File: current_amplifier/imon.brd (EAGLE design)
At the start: 160 x 100 mm, 32 parts, among them U1 AD8210, U2 AD1583_AD1583BRTZ-REEL7CT-ND, U3 FR014H5JZ, U4 OP-AMP_BALANCED, U6 LTC2312-12

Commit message: The imon current monitor board schematic is filled out
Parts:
- removed C1, C16, R2: (no value), rcl_custom:.0805-B
- removed U1: AD8210, marionette:SOIC-8_NARROW_BODY
- removed U3: FR014H5JZ, marionette:MLP-3X3
- added C105, C19: 1u, rcl_custom:.0402-B
- added C18, R12, R13, R19: np, rcl_custom:.0402-B
- added C20: 6.2n, rcl_custom:.0402-B
- added C50: 220p, rcl_custom:.0402-B
- added C80: 100n, rcl_custom:.0402-B
- added D1, D2: ESD8006-ESD8006, marionette:UDFN-8-3.3X1.0_6MIL
- added J1, R11, R16, R17: (no value), marionette:JUMPER-SHORTED-CUTTABLE-E0402-0.3MM
- added R10: 56, rcl_custom:.0402-B
- added R18: 1k, rcl_custom:.0402-B
- added R30: 51, rcl_custom:.0402-B
- added R40: 560, rcl_custom:.0402-B
- added R67, R9: np, rcl_custom:1206-0402
- added TP1, TP10, TP11, TP9: PAD+VIA_0.25MM, marionette:PAD+VIA_0.25MM
- added TP2: PAD+VIA_0.6MM, marionette:PAD+VIA_0.6MM
- added TP3, TP4, TP5, TP6, TP7, TP8: (no value), marionette:PAD-ROUND-1.0-NOCREAM+SILK
- added U$1: MCP1501", marionette:SOT23-6
- C10, C3: value (none) -> 100n; device rcl_custom:.0805-B -> rcl_custom:.0402-B
- C11, C12, C13, C14, C15, C4: value (none) -> 1u; device rcl_custom:.0805-B -> rcl_custom:.0402-B
- C2: value (none) -> 2.7n; device rcl_custom:.0805-B -> rcl_custom:.0402-B
- C5: value (none) -> 220p; device rcl_custom:.0805-B -> rcl_custom:.0402-B
- C6, C7: value (none) -> 1u; device rcl_custom:.0805-A-NOSILK -> rcl_custom:.0402-B
- C9: value (none) -> np
- R1: value (none) -> 97.6; device rcl_custom:.0805-B -> rcl_custom:.0402-B
- R3: value (none) -> 88.7; device rcl_custom:.0805-B -> rcl_custom:.0402-B
- R4: value (none) -> 976; device rcl_custom:.0805-B -> rcl_custom:.0402-B
- R5, R6: device rcl_custom:.0805-B -> rcl_custom:.0402-B
- R7, R8: device rcl_custom:.0805-B -> rcl_custom:1206-0402
- U2: value AD1583_AD1583BRTZ-REEL7CT-ND -> OPAMP_DUALFAN4852; device marionette:SOT23-3 -> marionette:MSOP-8
- U4: value OP-AMP_BALANCED -> AD8418; device marionette:SOIC-8 -> marionette:SOIC-8_BETTER_TOE
- moved R4 198.5 mm to (-69.8, -218.4)
- moved R5 167.5 mm to (-63.5, -191.8)
- moved R6 167.5 mm to (-63.5, -195.6)
- moved C2 164.9 mm to (-63.5, -170.2)
- moved R1 153.6 mm to (-63.5, -162.6)
- moved R3 142.3 mm to (-63.5, -158.8)
- moved C7 141.2 mm to (-63.5, -188.0)
- moved U2 137.0 mm to (-68.6, -212.1)
- moved C6 134.9 mm to (-63.5, -177.8)
- moved C5 127.2 mm to (-63.5, -166.4)
- moved C15 125.9 mm to (-63.5, -203.2)
- moved C14 125.9 mm to (-63.5, -199.4)
- moved U4 117.7 mm to (-57.1, -113.0)
- moved C4 112.1 mm to (-63.5, -147.3)
- moved C3 112.1 mm to (-63.5, -143.5)
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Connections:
- removed net N$15: R7.1, U1.8
- removed net N$7: R6.1, U4.5
- new net C80: C6.2, C80.2, U4.2
- new net N$11: R8.1, U4.1
- new net N$16: R5.2, R6.1, U$1.4
- new net N$17: C50.1, R30.1, U2.6
- new net N$18: C50.2, R16.2, R40.1, TP5.PAD, U2.7
- new net N$19: C18.2, R16.1, R17.2, U6.4
- new net N$20: D2.4, JP2.1, R11.2
- new net N$21: J1.1, R19.1, TP9.TP, U4.3
- new net N$22: R12.1, TP1.TP
- new net VREF_FILTERED: C105.2, C7.2, J1.2, R12.2, R13.1, R18.2, TP10.TP, TP11.TP, U4.7
- new net VREF_OUT: R18.1, U$1.1
- net GND: now also C105.1, C14.1, C15.1, C18.1, C19.2, C2.1, C20.1, C7.1, D1.10, D1.3, D1.6, D1.9, D2.10, D2.3, D2.6, D2.9, R13.2, R19.2, R5.1, U$1.2, U$1.3, U$1.5, U2.3, U2.4, U2.5; no longer C1.2, C14.2, C15.2, C16.1, C5.2, R3.1, R5.2, R6.2, U1.2, U1.3, U2.2, U4.4
- net N$1: now also R1.2, R11.1, TP3.PAD, U4.5; no longer JP2.1, R1.1, U1.5
- net N$10: now also R67.1, R8.2, R9.1; no longer C6.1, C7.1, R7.2
- net N$12: now also D1.4, TP8.PAD
- net N$13: now also D1.2, TP7.PAD
- net N$14: now also D1.1, TP6.PAD
- net N$2: now also C2.2, R1.1, R3.2, R4.2; no longer C1.1, C2.1, R1.2, R2.1
- net N$3: now also C5.1, R3.1, U2.2; no longer R2.2, U4.3
- net N$4: now also C5.2, R10.2, R4.1, TP4.PAD, U2.1; no longer R3.2, R4.2, U4.2
- net N$5: now also D2.1, R17.1; no longer C2.2, R4.1, U4.6, U6.4
- net N$6: now also C20.2, R10.1, R30.2, R40.2; no longer R5.1, U4.1
- net N$8: now also R7.1, U4.8; no longer R8.1, U1.1
- net N$9: now also R67.2, R7.2, R9.2; no longer C6.2, C7.2, R8.2
- net V3.3D: now also C19.1, D1.7
- net V5D: now also C14.2, C15.2, C6.1, C80.1, D1.5, R6.2, U$1.6, U2.8, U4.6; no longer C14.1, C15.1, C16.2, C5.1, U1.6, U2.3, U4.7
- net VREF_3.0V: now also TP2.TP; no longer U1.7, U2.1

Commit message: laying out imon.brd
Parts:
- removed D2: ESD8006-ESD8006, marionette:UDFN-8-3.3X1.0_6MIL
- removed JP3: (no value), pinhead:1X07
- removed U$1: MCP1501", marionette:SOT23-6
- added FIDUCIAL1, FIDUCIAL2, FIDUCIAL3, FIDUCIAL4, FIDUCIAL5, FIDUCIAL6: FIDUCIAL-1.0X2.5, marionette:FIDUCIAL-1.0X2.5
- added R14: np, rcl_custom:.0402-B
- added R2: (no value), marionette:JUMPER-SHORTED-CUTTABLE-E0402-0.3MM
- added TP12, TP14: PAD+VIA_0.25MM, marionette:PAD+VIA_0.25MM
- added TP13: PAD+VIA_GND_0.25MM, marionette:PAD+GND_VIA_0.25MM
- added U5: MCP1501", marionette:SOT23-6
- C13: value 1u -> 10u; device rcl_custom:.0402-B -> rcl_custom:.0805-B
- C8, R5: value (none) -> np
- JP2: device pinhead:1X04 -> pinhead:2X12/90
- R6: value (none) -> 10k
- TP11: value PAD+VIA_0.25MM -> PAD+VIA_0.6MM; device marionette:PAD+VIA_0.25MM -> marionette:PAD+VIA_0.6MM
- TP3: value (none) -> PAD+VIA_GND_0.25MM; device marionette:PAD-ROUND-1.0-NOCREAM+SILK -> marionette:PAD+GND_VIA_0.25MM
- moved TP11 393.4 mm to (24.4, 30.8)
- moved C105 380.2 mm to (27.0, 26.0), flipped to the bottom, turned to 90 degrees
- moved TP1 378.3 mm to (30.6, 30.1)
- moved R19 365.8 mm to (25.2, 24.3), flipped to the bottom
- moved J1 363.9 mm to (25.8, 26.0), flipped to the bottom, turned to 90 degrees
- moved TP10 362.0 mm to (29.4, 30.1)
- moved C19 351.5 mm to (53.2, 24.5), flipped to the bottom
- moved TP9 345.4 mm to (25.6, 21.5)
- moved R18 340.5 mm to (29.4, 26.0), flipped to the bottom, turned to 90 degrees
- moved TP4 330.6 mm to (43.1, 30.5)
- moved TP3 324.4 mm to (31.9, 31.6)
- moved TP6 322.7 mm to (93.0, -9.00)
- moved TP7 322.5 mm to (93.0, -13.0)
- moved TP8 322.3 mm to (93.0, -17.0)
- moved TP5 321.0 mm to (91.0, -6.00)
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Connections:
- net N$10 renamed VSHUNT_M
- net N$11 renamed VSHUNT_FILTERED_M
- net N$17 renamed FILTER2-
- net N$18 renamed FILTER_2_OUT
- net N$2 renamed FILTER_1_V1
- net N$21 renamed AD8418_REF2
- net N$22 renamed VREF_OPTIONAL
- net N$3 renamed FILTER1-
- net N$4 renamed FILTER_1_OUT
- net N$6 renamed FILTER_2_V1
- net N$8 renamed VSHUNT_FILTERED_P
- net N$9 renamed VSHUNT_P
- net VREF_3.0V renamed ADC_VREF
- removed net C80: C6.2, C80.2, U4.2
- removed net N$1: R1.2, R11.1, TP3.PAD, U4.5
- removed net N$12: D1.4, JP3.5, TP8.PAD, U6.6
- removed net N$13: D1.2, JP3.6, TP7.PAD, U6.7
- removed net N$14: D1.1, JP3.7, TP6.PAD, U6.8
- removed net N$16: R5.2, R6.1, U$1.4
- removed net N$19: C18.2, R16.1, R17.2, U6.4
- removed net N$20: D2.4, JP2.1, R11.2
- removed net N$5: D2.1, JP2.3, R17.1
- new net ADC_AIN: R2.1, U6.4
- new net ADC_CONV: D1.1, JP2.21, JP2.22, TP6.PAD, U6.8
- new net ADC_SCK: D1.2, JP2.19, JP2.20, TP7.PAD, U6.7
- new net ADC_SDO: D1.4, JP2.17, JP2.18, TP8.PAD, U6.6
- new net MCP1501_SHDN_N: R5.2, R6.1, U5.4
- new net VSHUNT_20X: R1.2, R11.1, TP12.TP, U4.5
- new net VSHUNT_20X_OUT: D1.8, JP2.3, JP2.4, R11.2
- new net VSHUNT_FILTERED: D1.5, JP2.5, JP2.6, R17.1
- new net VSHUNT_FILTERED_ADC: C18.2, R14.1, R16.1, R17.2, R2.2, TP14.TP
- net GND: now also C6.2, C80.2, JP2.1, JP2.11, JP2.12, JP2.15, JP2.16, JP2.23, JP2.24, JP2.7, JP2.8, R14.2, TP13.TP, TP3.TP, U4.2, U5.2, U5.3, U5.5; no longer D2.10, D2.3, D2.6, D2.9, JP2.4, JP3.2, JP3.4, U$1.2, U$1.3, U$1.5
- net V3.3D: now also JP2.13, JP2.14; no longer JP3.3
- net V5D: now also JP2.10, JP2.9, U5.6; no longer D1.5, JP3.1, U$1.6
- net VREF_OUT: now also U5.1; no longer U$1.1

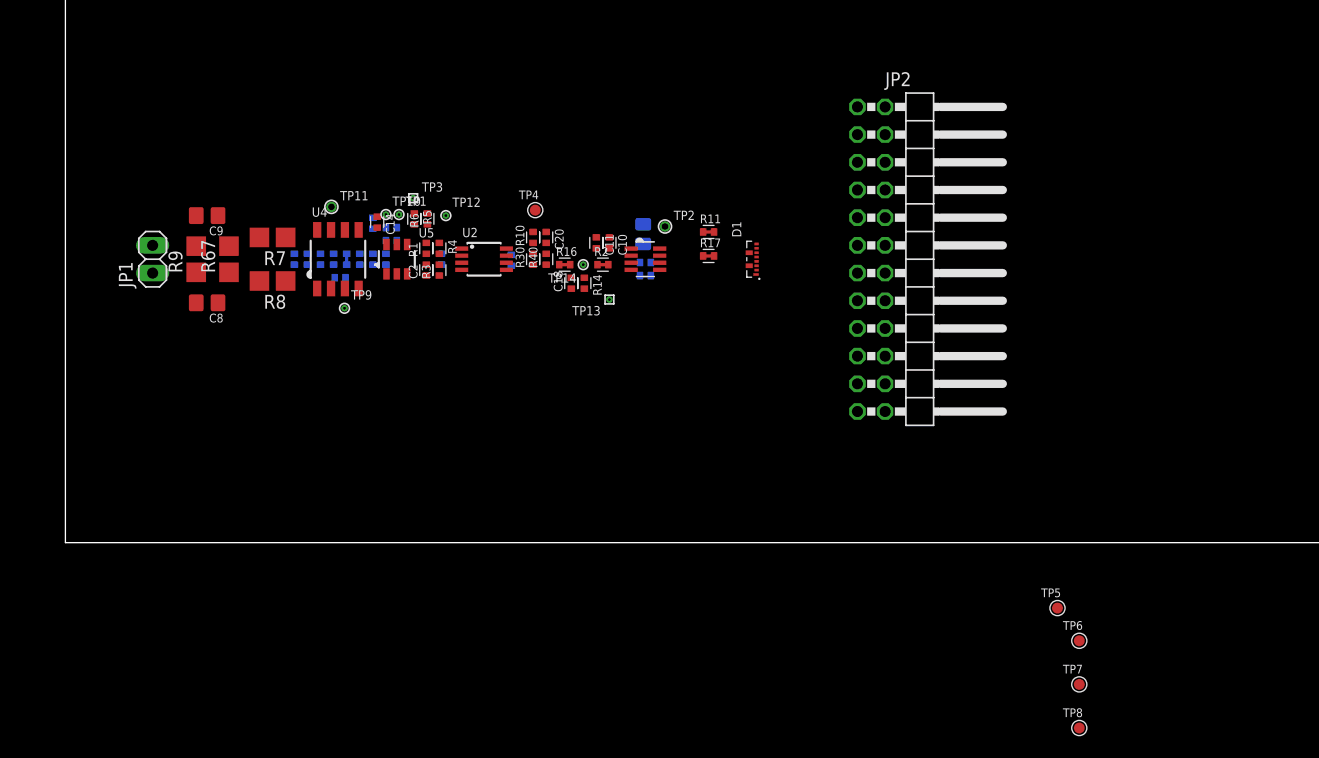
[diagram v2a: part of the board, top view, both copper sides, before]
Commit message: current monitor layout in progress
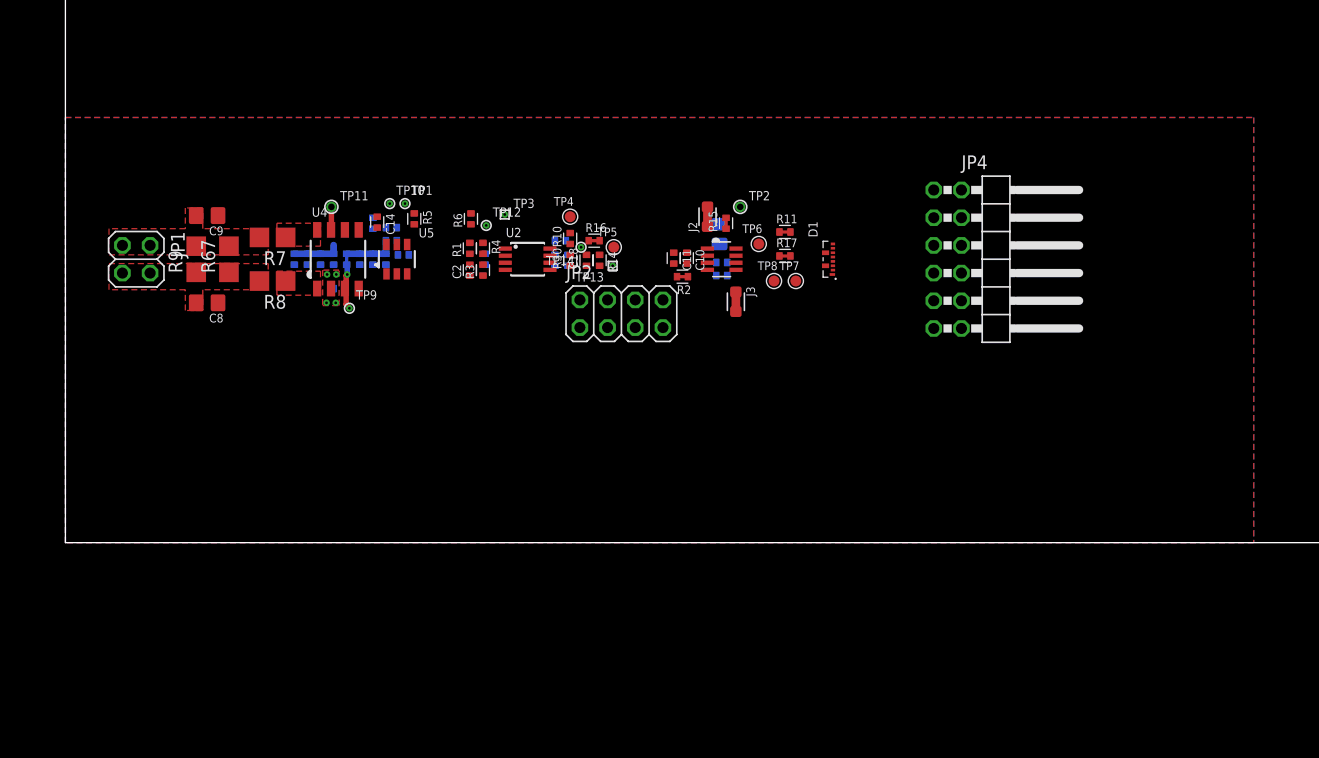
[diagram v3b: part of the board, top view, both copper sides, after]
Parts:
- added C1: 10n, rcl_custom:.0402-B
- added J2, J3: (no value), marionette:JUMPER-SHORTED-CUTTABLE-E0603-0.8MM
- added JP4: (no value), pinhead:2X06/90
- added R15: (no value), marionette:JUMPER-SHORTED-CUTTABLE-E0402-0.3MM
- JP1: device pinhead:1X02 -> pinhead:2X02
- JP2: device pinhead:2X12/90 -> pinhead:2X04
- moved TP5 52.5 mm to (50.3, 27.1)
- moved TP8 49.6 mm to (65.0, 24.0)
- moved TP6 46.8 mm to (63.6, 27.4)
- moved TP7 45.2 mm to (67.0, 24.0)
- moved JP2 28.4 mm to (51.0, 21.0), turned to 0 degrees
- moved TP3 8.53 mm to (40.3, 30.1)
- moved R2 7.38 mm to (56.6, 24.4), turned to 180 degrees
- moved C10 7.24 mm to (57.0, 26.1)
- moved C11 7.24 mm to (55.8, 26.1)
- moved TP2 7.13 mm to (61.9, 30.8)
- moved C12 7.00 mm to (60.2, 25.7)
- moved C13 7.00 mm to (60.0, 28.3)
- moved C19 7.00 mm to (60.2, 24.5)
- moved D1 7.00 mm to (70.0, 26.0)
- moved R11 7.00 mm to (66.0, 28.5)
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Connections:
- new net ADC_VREF_CUTTABLE: R15.1, U6.2
- new net V3.3D_CUTTABLE: J3.1, U6.5
- new net V5D_CUTTABLE: J2.1, U6.1
- net ADC_CONV: now also JP4.10, JP4.9; no longer JP2.21, JP2.22
- net ADC_SCK: now also JP4.7, JP4.8; no longer JP2.19, JP2.20
- net ADC_SDO: now also JP4.5, JP4.6; no longer JP2.17, JP2.18
- net ADC_VREF: now also R15.2; no longer U6.2
- net GND: now also C1.1, JP4.11, JP4.12; no longer JP2.1, JP2.11, JP2.12, JP2.15, JP2.16, JP2.2, JP2.23, JP2.24
- net V3.3D: now also J3.2, JP4.3, JP4.4; no longer JP2.13, JP2.14, U6.5
- net V5D: now also D1.8, J2.2, JP4.1, JP4.2; no longer JP2.10, JP2.9, U6.1
- net VREF_FILTERED: now also C1.2, JP2.5, JP2.6
- net VSHUNT_20X_OUT: now also JP2.1, JP2.2; no longer D1.8, JP2.3, JP2.4
- net VSHUNT_FILTERED: now also JP2.3, JP2.4; no longer D1.5, JP2.5, JP2.6
- net VSHUNT_M: now also JP1.3, JP1.4; no longer JP1.1
- net VSHUNT_P: now also JP1.1
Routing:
- net VREF_FILTERED: track 0.00 -> 6.94 mm
- net V5D: track 0.00 -> 4.42 mm
- net AD8418_REF2: track 0.00 -> 4.32 mm, vias 0 -> 1
- net GND: track 0.00 -> 0.20 mm, vias 0 -> 4
- added copper zone on layer 1, net GND
- added copper zone on layer 16, net GND
- added copper zone on layer 2, net GND
- added copper zone on layer 3, net N$1
- added copper zone on layer 1, net VSHUNT_FILTERED_M
- added copper zone on layer 1, net VSHUNT_FILTERED_P
- added copper zone on layer 1, net VSHUNT_M
- added copper zone on layer 1, net VSHUNT_P
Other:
- board text added: "Ground Clip Soldermask Areas"
- board text added: "Need some 1.1mm diameter vias for scope probes"

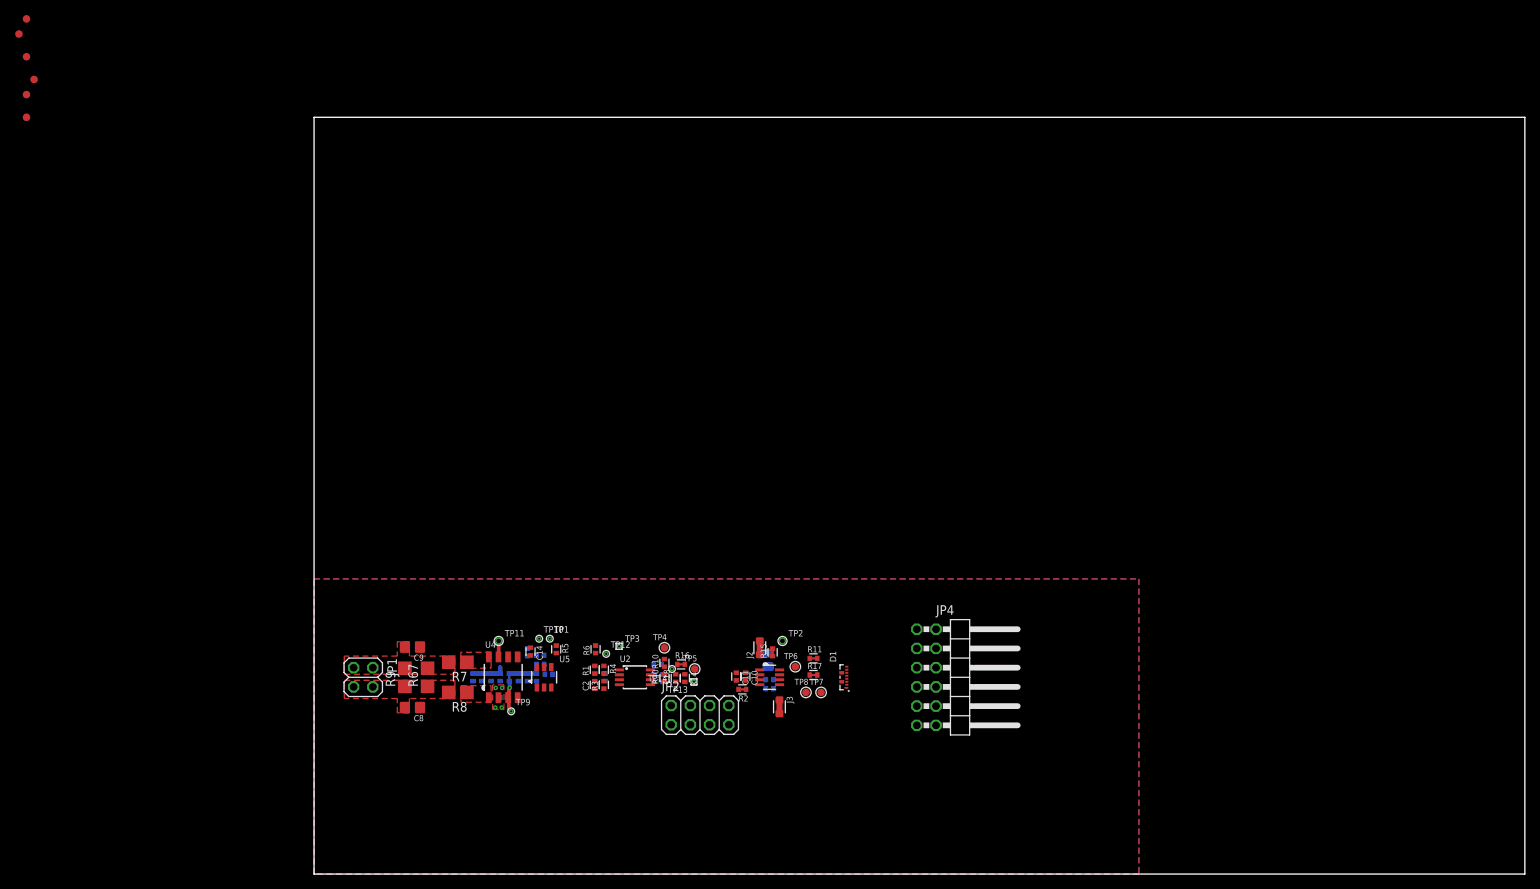
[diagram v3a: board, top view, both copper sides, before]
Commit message: The current monitor board is laid out but needs some polishing
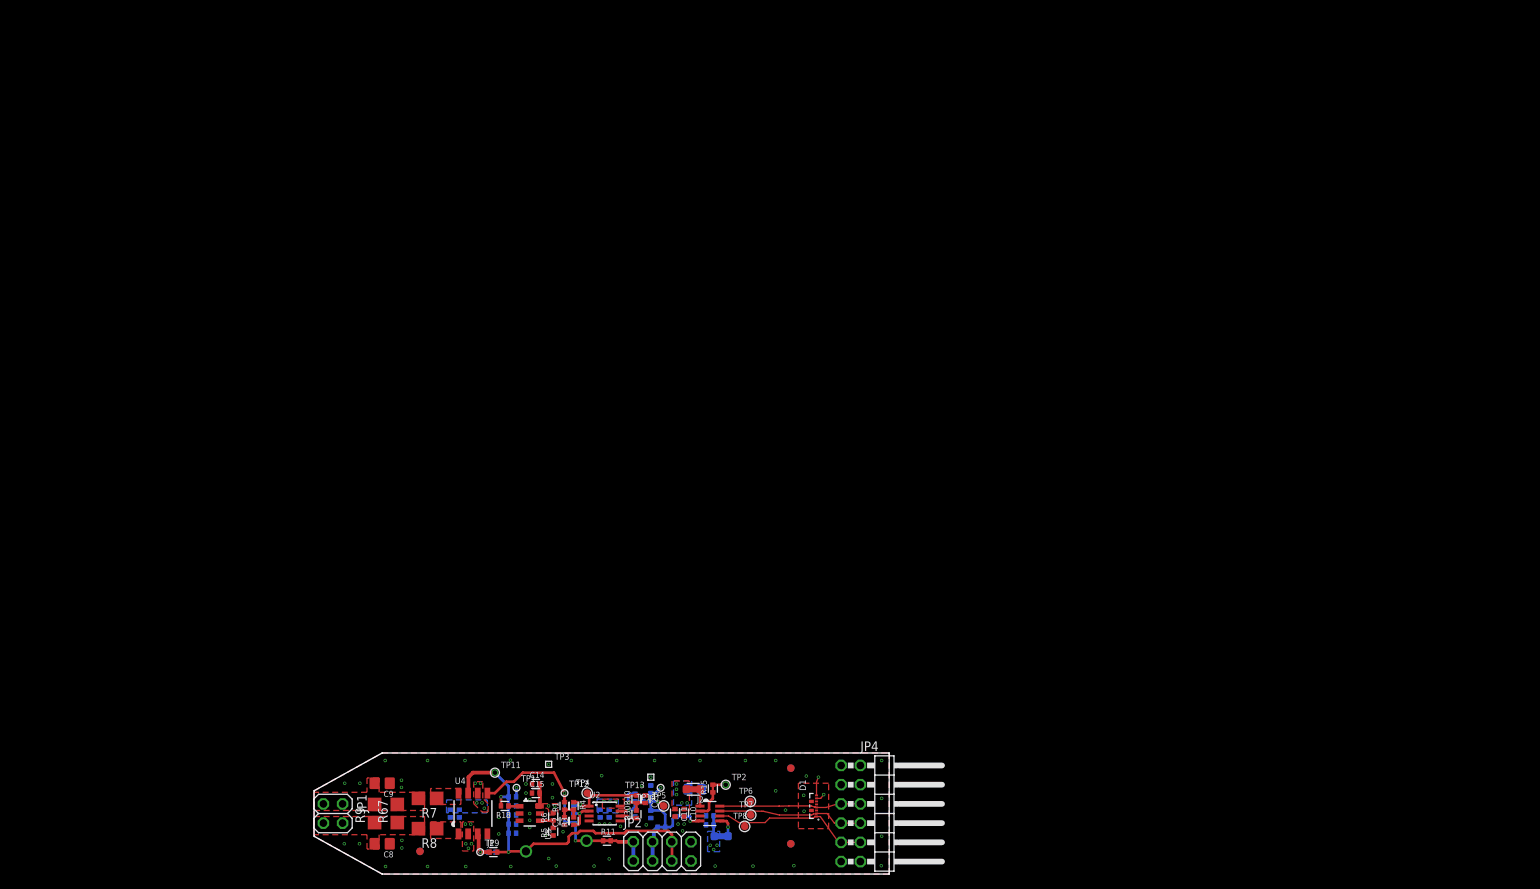
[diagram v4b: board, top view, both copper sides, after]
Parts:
- removed TP10: PAD+VIA_0.25MM, marionette:PAD+VIA_0.25MM
- moved FIDUCIAL2 147.8 mm to (63.0, 4.00), flipped to the bottom
- moved FIDUCIAL1 141.4 mm to (63.0, 14.0), flipped to the bottom
- moved FIDUCIAL5 141.4 mm to (63.0, 4.00)
- moved FIDUCIAL4 135.2 mm to (63.0, 14.0)
- moved FIDUCIAL3 117.2 mm to (14.0, 3.00), flipped to the bottom
- moved FIDUCIAL6 110.1 mm to (14.0, 3.00)
- moved R11 36.4 mm to (38.7, 4.40)
- moved R17 28.4 mm to (45.9, 6.20), flipped to the bottom, turned to 180 degrees
- moved R5 24.1 mm to (31.6, 5.60), turned to 90 degrees
- moved C3 23.8 mm to (39.0, 8.00)
- moved J1 23.2 mm to (23.7, 2.90), flipped to the top, turned to 0 degrees
- moved R6 22.8 mm to (31.6, 7.60)
- moved C4 22.3 mm to (37.8, 8.00)
- moved TP4 21.7 mm to (36.1, 10.7)
- moved J2 20.7 mm to (50.1, 11.2), turned to 180 degrees
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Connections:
- net ADC_CONV: now also D1.4, JP4.5, JP4.6; no longer D1.1, JP4.10, JP4.9
- net ADC_SDO: now also D1.1, JP4.10, JP4.9; no longer D1.4, JP4.5, JP4.6
- net VREF_FILTERED: no longer TP10.TP
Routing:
- net VREF_FILTERED: track 6.94 -> 48.0 mm, vias 0 -> 3
- net VSHUNT_20X: track 0.00 -> 25.6 mm, vias 0 -> 2
- net ADC_SDO: track 0.00 -> 21.4 mm
- net ADC_SCK: track 0.00 -> 19.9 mm
- net ADC_CONV: track 0.00 -> 19.4 mm
- net FILTER_1_OUT: track 0.00 -> 11.5 mm, vias 0 -> 1
- net VSHUNT_FILTERED_ADC: track 0.00 -> 11.3 mm
- net VSHUNT_20X_OUT: track 0.00 -> 6.61 mm
- net FILTER_2_V1: track 0.00 -> 6.14 mm, vias 0 -> 1
- net FILTER_2_OUT: track 0.00 -> 6.06 mm, vias 0 -> 2
- net VSHUNT_FILTERED: track 0.00 -> 4.85 mm
- net FILTER1-: track 0.00 -> 4.48 mm, vias 0 -> 1
- net V3.3D: track 0.00 -> 3.93 mm, vias 0 -> 4
- net ADC_VREF_CUTTABLE: track 0.00 -> 3.79 mm
- net FILTER_1_V1: track 0.00 -> 3.20 mm
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- added copper zone on layer 3, net GND
- added copper zone on layer 16, net V3.3D
- added copper zone on layer 3, net V3.3D
- added copper zone on layer 1, net V5D
- added copper zone on layer 16, net V5D
- added copper zone on layer 3, net V5D
- removed copper zone on layer 3, net N$1
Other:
- board size 160 x 100 mm -> 76 x 16 mm
- board text added: "CONV"
- board text added: "GND"
- board text added: "IMON"
- board text added: "SCK"
- board text added: "SDO"
- board text added: "V1.0"
- board text added: "V3.3D"
- board text added: "V5D"
